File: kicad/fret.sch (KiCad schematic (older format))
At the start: 41 parts, among them J1 +5V, J10 CONN_01X06, J2 GNDPWR, J3 +3.3V, J4 GND, J5 SDA, J6 SCL, J7 TEST, J8 ~RST, J9 GND, P0 TOUCH, P1 TOUCH, P2 TOUCH, P3 TOUCH, P4 TOUCH, P5 TOUCH, U1 MSP430G2553IRHB32

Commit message: kicad: Started layout
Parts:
- removed J9: GND, symbol CONN_01X01
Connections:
- net GND: now also C0.2, C1.2, C2.2, C3.2, C4.2, C5.2
- net GNDPWR: no longer C0.2, C1.2, C2.2, C3.2, C4.2, C5.2
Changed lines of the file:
@@
 LIBS:SparkFun
 LIBS:guitar-components
-LIBS:guitar-cache
+LIBS:fret-cache
 EELAYER 25 0
 EELAYER END
@@
 BUTTON
 $Comp
-L GNDPWR #PWR07
-U 1 1 556A8CC0
-P 1200 1850
-F 0 "#PWR07" H 1200 1900 40  0001 C CNN
-F 1 "GNDPWR" H 1200 1770 40  0001 C CNN
-F 2 "" H 1200 1850 60  0000 C CNN
-F 3 "" H 1200 1850 60  0000 C CNN
-	1    1200 1850
-	1    0    0    -1
-$EndComp
-$Comp
 L GNDPWR #PWR08
 U 1 1 556A8D01
@@
 	2950 2400 2650 2400
 $Comp
-L GNDPWR #PWR012
-U 1 1 556B2BA4
-P 1200 2900
-F 0 "#PWR012" H 1200 2950 40  0001 C CNN
-F 1 "GNDPWR" H 1200 2820 40  0001 C CNN
-F 2 "" H 1200 2900 60  0000 C CNN
-F 3 "" H 1200 2900 60  0000 C CNN
-	1    1200 2900
-	1    0    0    -1
-$EndComp
-$Comp
 L GNDPWR #PWR013
 U 1 1 556B2BAA
@@
 	2950 3450 2650 3450
 $Comp
-L GNDPWR #PWR016
-U 1 1 556B31E3
-P 1200 3950
-F 0 "#PWR016" H 1200 4000 40  0001 C CNN
-F 1 "GNDPWR" H 1200 3870 40  0001 C CNN
-F 2 "" H 1200 3950 60  0000 C CNN
-F 3 "" H 1200 3950 60  0000 C CNN
-	1    1200 3950
-	1    0    0    -1
-$EndComp
-$Comp
 L GNDPWR #PWR017
 U 1 1 556B31E9
@@
 	2950 4500 2650 4500
 $Comp
-L GNDPWR #PWR020
-U 1 1 556B3213
-P 1200 5000
-F 0 "#PWR020" H 1200 5050 40  0001 C CNN
-F 1 "GNDPWR" H 1200 4920 40  0001 C CNN
-F 2 "" H 1200 5000 60  0000 C CNN
-F 3 "" H 1200 5000 60  0000 C CNN
-	1    1200 5000
-	1    0    0    -1
-$EndComp
-$Comp
 L GNDPWR #PWR021
 U 1 1 556B3219
@@
 	2950 5550 2650 5550
 $Comp
-L GNDPWR #PWR024
-U 1 1 556B3764
-P 1200 6050
-F 0 "#PWR024" H 1200 6100 40  0001 C CNN
-F 1 "GNDPWR" H 1200 5970 40  0001 C CNN
-F 2 "" H 1200 6050 60  0000 C CNN
-F 3 "" H 1200 6050 60  0000 C CNN
-	1    1200 6050
-	1    0    0    -1
-$EndComp
-$Comp
 L GNDPWR #PWR025
 U 1 1 556B376A
@@
 	2950 6600 2650 6600
 $Comp
-L GNDPWR #PWR028
-U 1 1 556B3794
-P 1200 7100
-F 0 "#PWR028" H 1200 7150 40  0001 C CNN
-F 1 "GNDPWR" H 1200 7020 40  0001 C CNN
-F 2 "" H 1200 7100 60  0000 C CNN
-F 3 "" H 1200 7100 60  0000 C CNN
-	1    1200 7100
-	1    0    0    -1
-$EndComp
-$Comp
 L GNDPWR #PWR029
 U 1 1 556B379A
@@
 Connection ~ 4500 3550
 $Comp
-L CONN_01X01 J9
-U 1 1 556B48E5
-P 3950 3650
-F 0 "J9" H 3950 3750 50  0001 C CNN
-F 1 "GND" H 4050 3650 50  0000 L CNN
-F 2 "" H 3950 3650 60  0000 C CNN
-F 3 "" H 3950 3650 60  0000 C CNN
-	1    3950 3650
-	-1   0    0    1
-$EndComp
-$Comp
-L GND #PWR039
-U 1 1 556B5288
-P 4250 3750
-F 0 "#PWR039" H 4250 3750 30  0001 C CNN
-F 1 "GND" H 4250 3680 30  0001 C CNN
-F 2 "" H 4250 3750 60  0000 C CNN
-F 3 "" H 4250 3750 60  0000 C CNN
-	1    4250 3750
-	1    0    0    -1
-$EndComp
-Wire Wire Line
-	4150 3650 4250 3650
-Wire Wire Line
-	4250 3650 4250 3750
+L GND #PWR?
+U 1 1 556AA489
+P 1200 3950
+F 0 "#PWR?" H 1200 3950 30  0001 C CNN
+F 1 "GND" H 1200 3880 30  0001 C CNN
+F 2 "" H 1200 3950 60  0000 C CNN
+F 3 "" H 1200 3950 60  0000 C CNN
+	1    1200 3950
+	1    0    0    -1
+$EndComp
+$Comp
+L GND #PWR?
+U 1 1 556AA9AF
+P 1200 1850
+F 0 "#PWR?" H 1200 1850 30  0001 C CNN
+F 1 "GND" H 1200 1780 30  0001 C CNN
+F 2 "" H 1200 1850 60  0000 C CNN
+F 3 "" H 1200 1850 60  0000 C CNN
+	1    1200 1850
+	1    0    0    -1
+$EndComp
+$Comp
+L GND #PWR?
+U 1 1 556AA9EE
+P 1200 2900
+F 0 "#PWR?" H 1200 2900 30  0001 C CNN
+F 1 "GND" H 1200 2830 30  0001 C CNN
+F 2 "" H 1200 2900 60  0000 C CNN
+F 3 "" H 1200 2900 60  0000 C CNN
+	1    1200 2900
+	1    0    0    -1
+$EndComp
+$Comp
+L GND #PWR?
+U 1 1 556AACA1
+P 1200 5000
+F 0 "#PWR?" H 1200 5000 30  0001 C CNN
+F 1 "GND" H 1200 4930 30  0001 C CNN
+F 2 "" H 1200 5000 60  0000 C CNN
+F 3 "" H 1200 5000 60  0000 C CNN
+	1    1200 5000
+	1    0    0    -1
+$EndComp
+$Comp
+L GND #PWR?
+U 1 1 556AADFE
+P 1200 6050
+F 0 "#PWR?" H 1200 6050 30  0001 C CNN
+F 1 "GND" H 1200 5980 30  0001 C CNN
+F 2 "" H 1200 6050 60  0000 C CNN
+F 3 "" H 1200 6050 60  0000 C CNN
+	1    1200 6050
+	1    0    0    -1
+$EndComp
+$Comp
+L GND #PWR?
+U 1 1 556AAF41
+P 1200 7100
+F 0 "#PWR?" H 1200 7100 30  0001 C CNN
+F 1 "GND" H 1200 7030 30  0001 C CNN
+F 2 "" H 1200 7100 60  0000 C CNN
+F 3 "" H 1200 7100 60  0000 C CNN
+	1    1200 7100
+	1    0    0    -1
+$EndComp
 $EndSCHEMATC

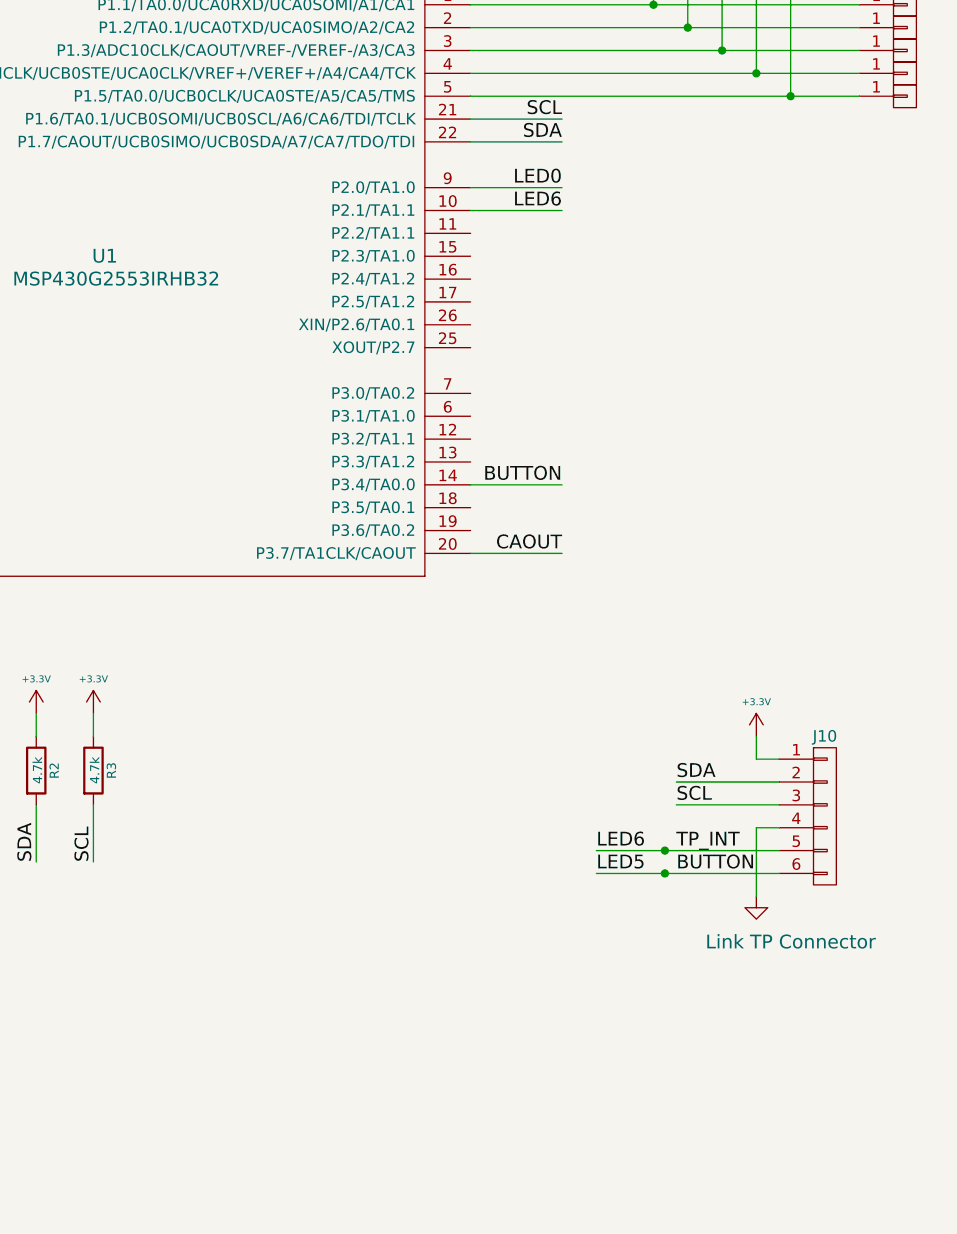
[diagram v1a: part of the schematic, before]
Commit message: kicad: almost finished layout with the msp430
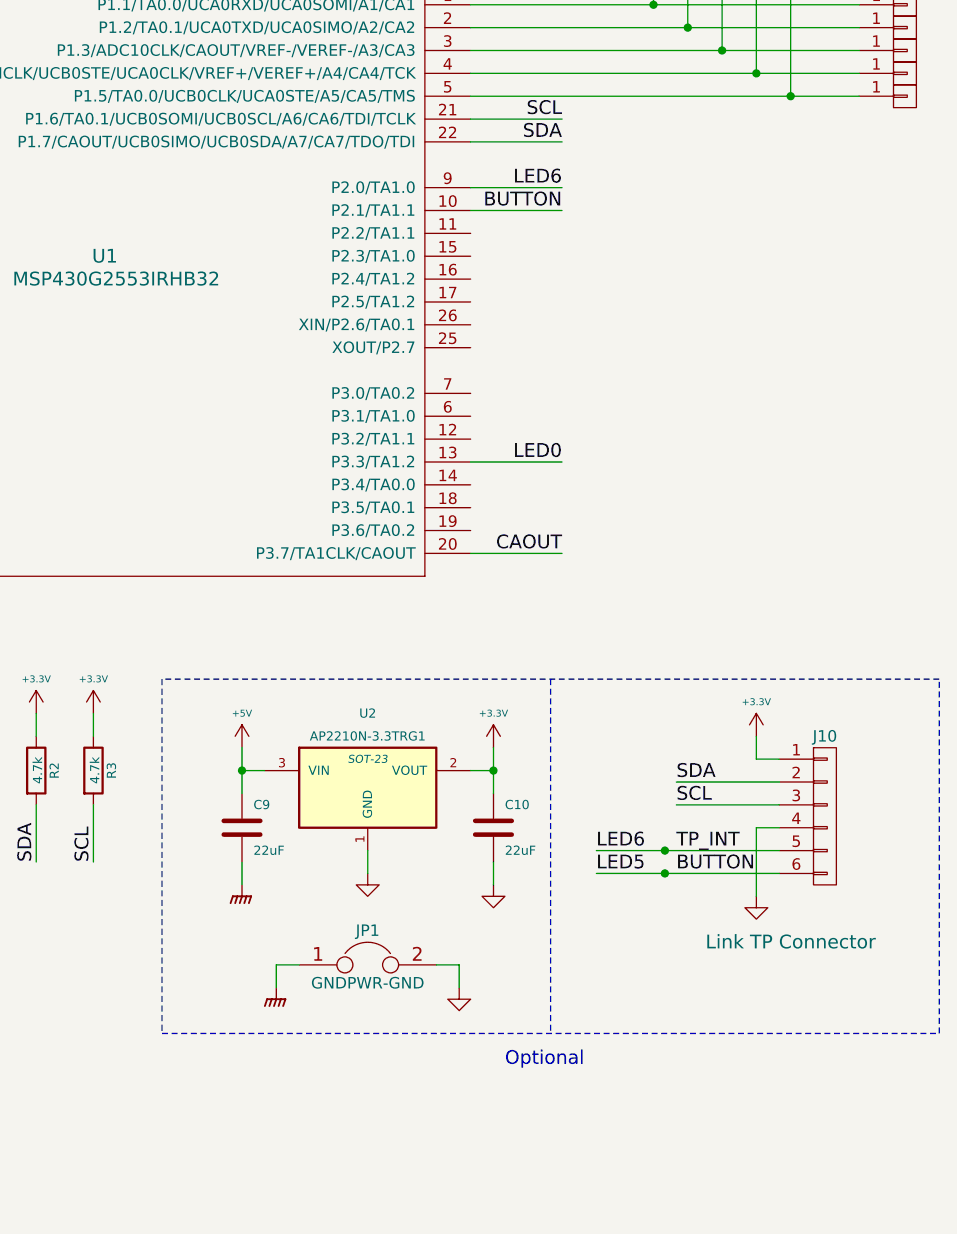
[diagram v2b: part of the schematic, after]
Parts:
- added C10, C9: 22uF, symbol C
- added JP1: GNDPWR-GND, symbol JUMPER
- added U2: AP2210N-3.3TRG1, SOT-23, symbol APE8865N-33-HF-3
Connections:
- net +3V3: now also C10.1, U2.2 (VOUT)
- net +5V: now also C9.1, U2.3 (VIN)
- net BUTTON: now also U1.10 (P2.1/TA1.1); no longer U1.14 (P3.4/TA0.0)
- net GND: now also C10.2, JP1.2, U2.1 (GND)
- net GNDPWR: now also C9.2, JP1.1
- net LED0: now also U1.13 (P3.3/TA1.2); no longer U1.9 (P2.0/TA1.0)
- net LED6: now also U1.9 (P2.0/TA1.0); no longer U1.10 (P2.1/TA1.1)
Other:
- note added: "Optional"

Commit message: kicad: finished stm32 schematics
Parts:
- removed U1: MSP430G2553IRHB32, symbol MSP430G2553IRHB32
- added C?: 100nF, symbol C
- added C? (x2): 47nF, symbol C
- added J?: SWCLK, symbol CONN_01X01
- added J?: SWDIO, symbol CONN_01X01
- added R?: 10k, symbol R
- added R? (x2): 0, symbol R
- added U?: STM32F051K*T, symbol STM32F051K
- C6: value 1uF -> 100nF
- C8: value 1nF -> 100nF
- J7: value TEST -> BOOT0
- J8: value ~RST -> NRST
- R4, R5, R6, R7, R8, R9: value 47k -> 10k
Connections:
- net +3V3: now also C?.1, U?.1 (VDD), U?.17 (VDD), U?.5 (VDDA)
- net BUTTON: now also U?.11 (PA5)
- net GND: now also C?.2, C?.2, C?.2, R?.1, U?.16 (VSS), U?.32 (VSS)
- net LED0: now also U?.13 (PA7)
- net LED6: now also U?.12 (PA6)
- net SCL: now also R?.2, U?.29 (PB6)
- net SDA: now also R?.2, U?.30 (PB7)
- net at P1.1 (P1): now also R5.2; no longer R5.1
- net at P2.1 (P1): now also R6.2; no longer R6.1
- net at P3.1 (P1): now also R7.2; no longer R7.1
- net at P0.1 (P1): now also R4.2; no longer R4.1
- net at P4.1 (P1): now also R8.2; no longer R8.1
- net at P5.1 (P1): now also R9.2; no longer R9.1
- removed net CAOUT: R4.2, R5.2, R6.2, R7.2, R8.2, R9.2
- net TEST renamed BOOT0
- net BOOT0: now also R?.2, U?.31 (BOOT0)
- net ~RST renamed NRST
- net NRST: now also U?.4 (NRST)
- new net: R4.1, U?.6 (PA0)
- new net: R5.1, U?.7 (PA1)
- new net: R6.1, U?.8 (PA2)
- new net: R7.1, U?.19 (PA9)
- new net: R8.1, U?.20 (PA10)
- new net: R9.1, U?.21 (PA11)
- new net: C?.1, U?.22 (PA12)
- new net: C?.1, U?.9 (PA3)
- new net MISO: R?.1, U?.27 (PB4), U?.28 (PB5)
- new net SCK: R?.1, U?.26 (PB3)
- new net SWCLK: J?.1 (P1), U?.24 (PA14)
- new net SWDIO: J?.1 (P1), U?.25 (PA15)
- no-connect marks 0 -> 2
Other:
- note added: "/RX"
- note added: "/TX"
- note added: "I2C1/USART1"
- note added: "SPI1"
- note added: "SPI1_MOSI"
- note added: "TSC_G1"
- note added: "TSC_G4"
- moved on the sheet: C6, C7, C8, R1, R4, R5, R6, R7, R8, R9

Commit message: kicad: started fret layout with stm32
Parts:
- removed R? (x2): 0, symbol R
- added JP2: SCK-CONNECTION, symbol JUMPER
- added JP3: SPI-CONNECTION, symbol JUMPER
- gave numbers to parts that had none: 7
- renumbered C8 to C11, R4 to R0, R5 to R1, R6 to R2, R7 to R3, R8 to R4, R9 to R5, R1 to R6, R2 to R7, R3 to R8
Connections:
- net BUTTON: now also U1.12 (PA6); no longer U1.11 (PA5)
- net LED6: now also U1.11 (PA5); no longer U1.12 (PA6)
- net MISO: now also JP3.1
- net SCK: now also JP2.1
- net SCL: now also JP2.2
- net SDA: now also JP3.2
- no-connect marks 2 -> 7

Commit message: kicad: layout was almost finished a while ago
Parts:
- removed JP2: SCK-CONNECTION, symbol JUMPER
- C0, C1, C11, C2, C3, C4, C5, C6, C7, C8: footprint (none) -> Capacitors_SMD:C_0603; Digi-Key Page (none) -> 100nF
- C10, C9: footprint (none) -> Capacitors_SMD:C_0805; Digi-Key Page (none) -> 22nF
- C12, C13: footprint (none) -> Capacitors_SMD:C_0603; Digi-Key Page (none) -> 47nF
- J1, J2, J3, J4, J5, J6: footprint (none) -> guitar-components:IDC-1x1; Digi-Key Page (none) -> http://www.digikey.com/product-search/en?vendor=0&keywords=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
- J10: footprint (none) -> Connectors_Molex:Connector_Molex_PicoBlade_53261-0471; Digi-Key Page (none) -> todo
- J11, J7, J8, J9: footprint (none) -> guitar-components:pad-2mm-round; Digi-Key Page (none) -> n/a
- JP1: footprint (none) -> Resistors_SMD:R_0603; Digi-Key Page (none) -> 0ohm
- JP2: renamed from JP3; footprint (none) -> Resistors_SMD:R_0603; Digi-Key Page (none) -> 0ohm
- LED0, LED1, LED2, LED3, LED4, LED5: footprint (none) -> guitar-components:5050-6pin
- P0, P1, P2, P3, P4, P5: footprint (none) -> guitar-components:TP-8x15; Digi-Key Page (none) -> n/a
- R0, R1, R12, R2, R3, R4, R5, R6: footprint (none) -> Resistors_SMD:R_0603; Digi-Key Page (none) -> 10k
- R7, R8: footprint (none) -> Resistors_SMD:R_0603; Digi-Key Page (none) -> 4.7k
- U1: footprint (none) -> Housings_QFP:LQFP-32_7x7mm_Pitch0.8mm; Digi-Key Page (none) -> http://www.digikey.com/product-detail/en/STM32F051K8T6/497-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
- U2: footprint SOT-23 -> Housings_SOT-23_SOT-143_TSOT-6:SOT-23; Digi-Key Page (none) -> http://www.digikey.com/product-detail/en/AP2210N-3.3TRG1/AP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
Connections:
- net SCL is gone; now on net SCK: J10.3 (P3), J6.1 (P1), R8.2, U1.29 (PB6)
- net P0: now reaches R0.1, U1.6 (PA0)
- net P1: now reaches R1.1, U1.7 (PA1)
- net P2: now reaches R2.1, U1.8 (PA2)
- net P3: now reaches R3.1, U1.19 (PA9)
- net P4: now reaches R4.1, U1.20 (PA10)
- net P5: now reaches R5.1, U1.21 (PA11)
- net CG4: now reaches C13.1, U1.22 (PA12)
- net CG1: now reaches C12.1, U1.9 (PA3)
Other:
- moved on the sheet: P0, P1, P2, P3, P4, P5, R0, R1, R2, R3, R4, R5

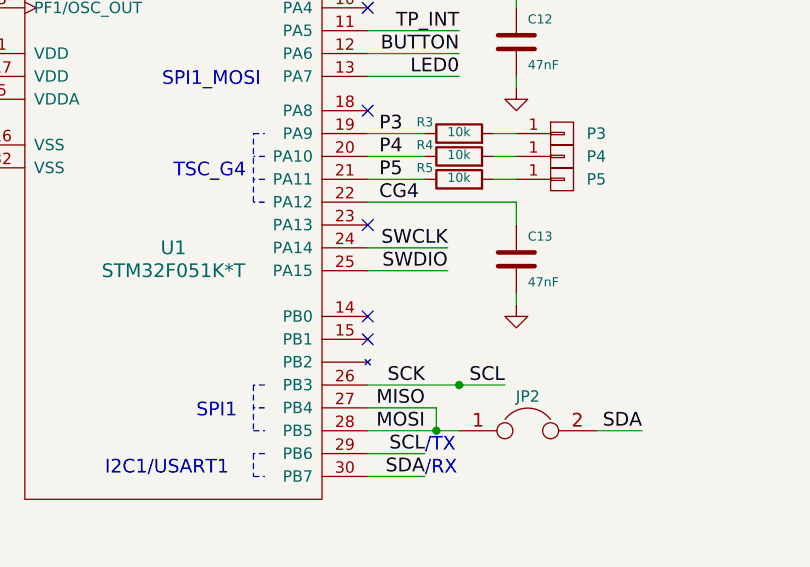
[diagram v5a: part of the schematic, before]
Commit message: kicad: Ordered fret board
Board modifications:
* SWDIO now in the right spot
* Silkscreen adjustments
* Testing touchpad silkscreen edge effects on the backend

Board is v2.0

Sent order to elecrow.
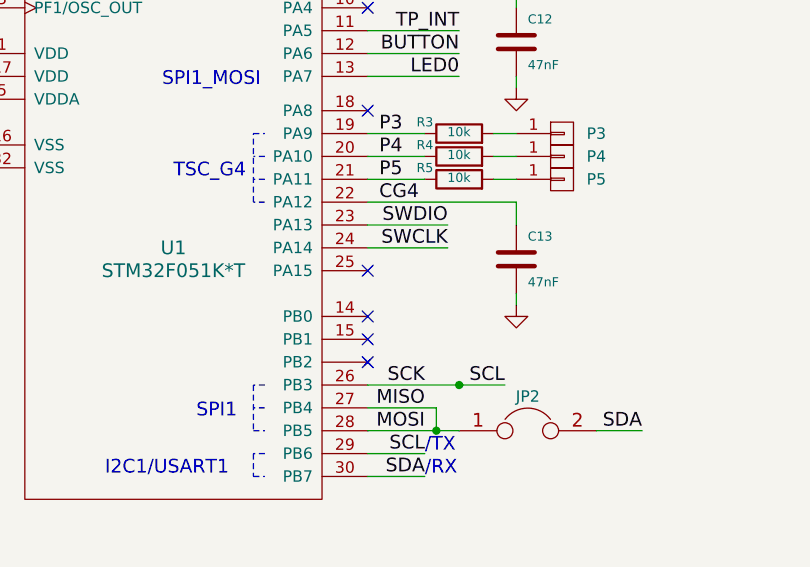
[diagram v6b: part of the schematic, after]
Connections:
- net SWDIO: now also U1.23 (PA13); no longer U1.25 (PA15)
- no-connect marks 7 -> 8
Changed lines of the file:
@@
 Text Label 7700 2750 2    60   ~ 0
 SWCLK
-Text Label 7700 2850 2    60   ~ 0
+Text Label 7700 2650 2    60   ~ 0
 SWDIO
 Text Label 4650 3050 2    60   ~ 0
@@
 	7350 2750 7700 2750
 Wire Wire Line
-	7700 2850 7350 2850
-Wire Wire Line
 	4300 3050 4650 3050
 Wire Wire Line
@@
 NoConn ~ 7350 1700
 NoConn ~ 7350 2150
-NoConn ~ 7350 2650
+NoConn ~ 7350 2850
 NoConn ~ 7350 3050
 NoConn ~ 7350 3150
@@
 CG4
 Connection ~ 7750 3350
+Wire Wire Line
+	7700 2650 7350 2650
+NoConn ~ 7350 3250
 $EndSCHEMATC
